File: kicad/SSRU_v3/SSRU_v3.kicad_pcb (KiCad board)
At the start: 2 copper layers, 100 x 100 mm, 122 parts, among them J1 AVR-ISP-6, J10 Conn_01x04, J11 Conn_01x02, J20 Conn_01x02, J21 Conn_01x02, J22 Conn_01x04, J23 Conn_01x02, J24 Conn_01x04, J25 Conn_01x02, J26 Conn_01x03, J27 Conn_01x03, J28 Conn_01x02, J29 Conn_01x02, J3 Conn_01x02, J30 Conn_01x02, J4 Conn_01x02, J5 Conn_01x02, J8 Conn_01x02, J9 Conn_01x02, SW1 SW_Push, U1 MCP2515-xSO, U10 TJA1051T, U11 Ai-Thinker-Ra-02, U12 TJA1051T, U2 ATmega328P-A, U3 TXS0102DCT, U4 LM2576S-5, U5 AMS1117-3.3, U6 LM324, U7 MCP2515-xSO, U8 74LVC1G17, U9 MT3608/SDB628, Y1 16MHz, Y3 16MHz, Y4 16MHz

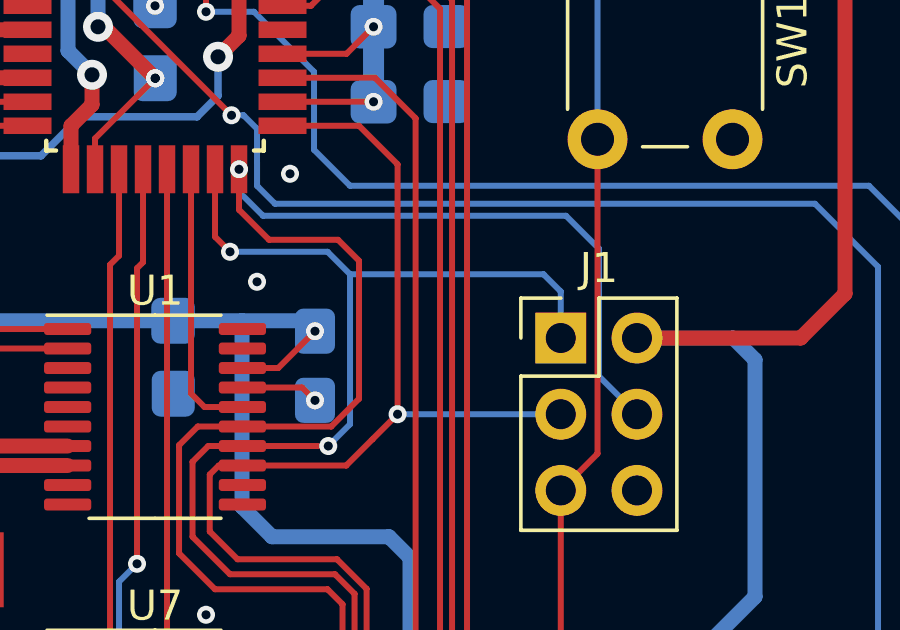
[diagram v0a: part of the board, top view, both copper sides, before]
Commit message: ssru v3
current to voltage lm324 supply to  5v. icsp header mosi miso fixed
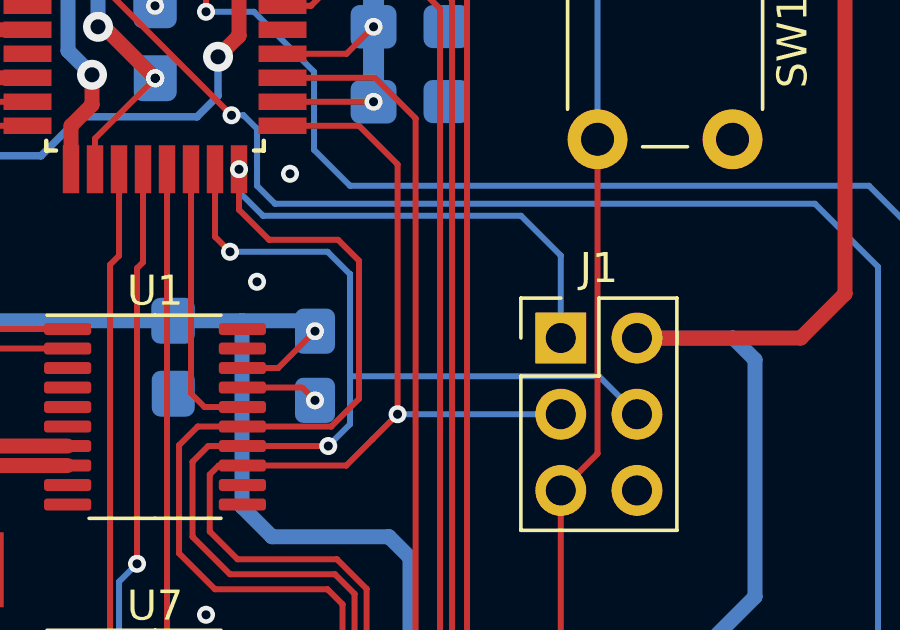
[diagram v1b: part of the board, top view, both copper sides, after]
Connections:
- C21 pad 1: +3.3V -> +5V
- J1 pad 1: MOSI -> MISO
- J1 pad 4: MISO -> MOSI
- U6 pad 4: +3.3V -> +5V
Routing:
- net MOSI: track 78.9 -> 83.6 mm
- net MISO: track 88.4 -> 84.0 mm
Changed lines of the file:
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@@
 			(layers "*.Cu" "*.Mask")
 			(remove_unused_layers no)
-			(net 36 "MOSI")
+			(net 30 "MISO")
 			(pinfunction "MISO")
 			(pintype "passive")
@@
 			(layers "*.Cu" "*.Mask")
 			(remove_unused_layers no)
-			(net 30 "MISO")
+			(net 36 "MOSI")
 			(pinfunction "MOSI")
 			(pintype "passive")
@@
 			(layers "F.Cu" "F.Mask" "F.Paste")
 			(roundrect_rratio 0.15)
-			(net 1 "+3.3V")
+			(net 3 "+5V")
 			(pinfunction "V+")
 			(pintype "power_in")
@@
 			(layers "B.Cu" "B.Mask" "B.Paste")
 			(roundrect_rratio 0.212766)
-			(net 1 "+3.3V")
+			(net 3 "+5V")
 			(pintype "passive")
 		)
@@
 	)
 	(segment
-		(start 164.8 106.9)
-		(end 163.7 105.8)
+		(start 163.525 107.125)
+		(end 162.2 105.8)
 		(width 0.2)
 		(layer "B.Cu")
@@
 	)
 	(segment
-		(start 163.7 105.8)
-		(end 153.6 105.8)
-		(width 0.2)
-		(layer "B.Cu")
-		(net 30)
-	)
-	(segment
-		(start 164.8 111.15)
-		(end 164.8 106.9)
+		(start 153.6 105.8)
+		(end 152.8 105)
 		(width 0.2)
 		(layer "B.Cu")
@@
 	)
 	(segment
-		(start 153.6 105.8)
-		(end 152.8 105)
+		(start 162.2 105.8)
+		(end 153.6 105.8)
 		(width 0.2)
 		(layer "B.Cu")
@@
 	)
 	(segment
-		(start 166.065 112.415)
-		(end 164.8 111.15)
+		(start 163.525 109.875)
+		(end 163.525 107.125)
 		(width 0.2)
 		(layer "B.Cu")
@@
 	(segment
 		(start 156.5 107.75)
-		(end 162.95 107.75)
+		(end 155.75 107)
 		(width 0.2)
 		(layer "B.Cu")
@@
 	)
 	(segment
-		(start 156.5 107.75)
-		(end 155.75 107)
+		(start 164.8 111.15)
+		(end 166.065 112.415)
 		(width 0.2)
 		(layer "B.Cu")
@@
 	)
 	(segment
-		(start 155.75 107)
-		(end 152.5 107)
+		(start 156.5 107.75)
+		(end 156.5 111.15)
 		(width 0.2)
 		(layer "B.Cu")
@@
 	)
 	(segment
-		(start 163.525 108.325)
-		(end 163.525 109.875)
+		(start 155.75 107)
+		(end 152.5 107)
 		(width 0.2)
 		(layer "B.Cu")
@@
 	)
 	(segment
-		(start 162.95 107.75)
-		(end 163.525 108.325)
+		(start 156.5 111.15)
+		(end 164.8 111.15)
 		(width 0.2)
 		(layer "B.Cu")

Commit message: SSRU new layout
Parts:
- removed C37, C47: 100nF, RMC_Capacitor:C_0805_2012Metric_Pad1.18x1.45mm_HandSolder_L
- removed J28, J29: Conn_01x02, Connector_JST:JST_XH_B2B-XH-A_1x02_P2.50mm_Vertical
- added C15: 100nF, RMC_Capacitor:C_0805_2012Metric_Pad1.18x1.45mm_HandSolder_L, B.Cu at (120.0, 127.0)
- added C16: 100nF, RMC_Capacitor:C_0805_2012Metric_Pad1.18x1.45mm_HandSolder_L, B.Cu at (116.0, 127.0)
- added D6: SMA Diode, Diode_SMD:D_SMA_Handsoldering, F.Cu at (125.0, 125.0)
- added F3: Fuse, to be sorted:Fuse_1210_3225Metric_Pad1.42x2.65mm_HandSolder, F.Cu at (125.0, 135.0)
- added J31: Conn_01x04, Connector_JST:JST_XH_B4B-XH-A_1x04_P2.50mm_Vertical, F.Cu at (117.0, 146.0)
- added U13: CH340N, Package_SO:SOP-8_3.9x4.9mm_P1.27mm, F.Cu at (118.0, 134.0)
- C11, C7: footprint Capacitor_THT:CP_Radial_D6.3mm_P2.50mm -> RMC_Capacitor:CP_Radial_D6.3mm_P2.50mm_handsolder
- C28, C29, C31, C36, R1, R28, R29, R30, R31, R32, R33, R34, R35, R37: moved to F.Cu
- C46: value 0.1uF -> 100nF
- F1, F2: footprint Fuse:Fuse_1210_3225Metric_Pad1.42x2.65mm_HandSolder -> to be sorted:Fuse_1210_3225Metric_Pad1.42x2.65mm_HandSolder
- U2: footprint Package_QFP:TQFP-32_7x7mm_P0.8mm -> RMC_QFP:TQFP-32_7x7mm_P0.8mm_L
- U3: footprint Package_SO:SSOP-8_2.95x2.8mm_P0.65mm -> RMC_SO:SOIC-8_3.9x4.9mm_P1.27mm_RMC_Handsolder
- U8: footprint Package_TO_SOT_SMD:SOT-23-5_HandSoldering -> RMC_SOT:SOT-23-5_HandSoldering_Extended_RMC
- U9: footprint Package_TO_SOT_SMD:SOT-23-6_Handsoldering -> RMC_SOT:SOT-23-6_Handsoldering_Extended_RMC
- moved C10 163.0 mm to (53.0, 24.0), turned to -90 degrees
- moved F1 159.4 mm to (48.0, 23.0), turned to -90 degrees
- moved R39 158.7 mm to (55.8, 17.1)
- moved C9 157.4 mm to (56.0, 24.0), turned to 90 degrees
- moved D4 155.9 mm to (62.0, 17.0)
- moved C8 155.2 mm to (55.0, 28.0), turned to 0 degrees
- moved D3 147.8 mm to (54.5, 44.0), turned to -90 degrees
- moved R38 145.9 mm to (51.5, 44.0), turned to -90 degrees
- moved U5 145.3 mm to (65.0, 25.0), turned to 0 degrees
- moved G*** 106.9 mm to (40.1, 96.5)
- moved R23 104.4 mm to (51.0, 66.0), turned to 0 degrees
- moved C35 104.1 mm to (54.0, 60.0), turned to 180 degrees
- moved J30 102.5 mm to (197.0, 84.0)
- moved D5 101.0 mm to (53.0, 57.0), turned to 180 degrees
- moved C33 99.6 mm to (54.0, 63.0), turned to 0 degrees
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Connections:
- net PUMP_THERM_IN renamed PUMP_NTC_100k
- U2 pad 12: LVB_TEMP -> CS_CAN1
- U2 pad 13: CS_CAN1 -> CS_CAN2
- U2 pad 14: CS_CAN2 -> CS_CAN3
- U2 pad 19: POT3_IN -> POT2_IN
- U2 pad 22: POT4_IN -> POT1_IN
- U2 pad 23: POT2_IN -> LVB_TEMP
- U2 pad 24: POT1_IN -> IRO
- U2 pad 30: CS_CAN3 -> 328_RX
- U2 pad 31: IRO -> 328_TX
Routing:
- net +5V: track 362.5 -> 0.00 mm, vias 8 -> 0
- net +3.3V: track 298.4 -> 0.00 mm, vias 8 -> 0
- net RST: track 91.4 -> 0.00 mm, vias 2 -> 0
- net PUMP_NTC_100k: track 85.6 -> 0.00 mm, vias 2 -> 0
- net MISO: track 84.0 -> 0.00 mm, vias 1 -> 0
- net MOSI: track 83.6 -> 0.00 mm, vias 4 -> 0
- net CS_CAN3: track 82.5 -> 0.00 mm, vias 2 -> 0
- net POT3_IN: track 80.2 -> 0.00 mm, vias 1 -> 0
- net POT4_IN: track 78.1 -> 0.00 mm, vias 1 -> 0
- net LVB_TEMP: track 74.2 -> 0.00 mm, vias 3 -> 0
- net SCK: track 73.0 -> 0.00 mm, vias 1 -> 0
- net +24V: track 72.2 -> 0.00 mm
- net POT2_IN: track 71.3 -> 0.00 mm, vias 1 -> 0
- net IRO: track 70.9 -> 0.00 mm, vias 2 -> 0
- net BRAKE_TEMP_OUT4: track 70.0 -> 0.00 mm, vias 4 -> 0
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
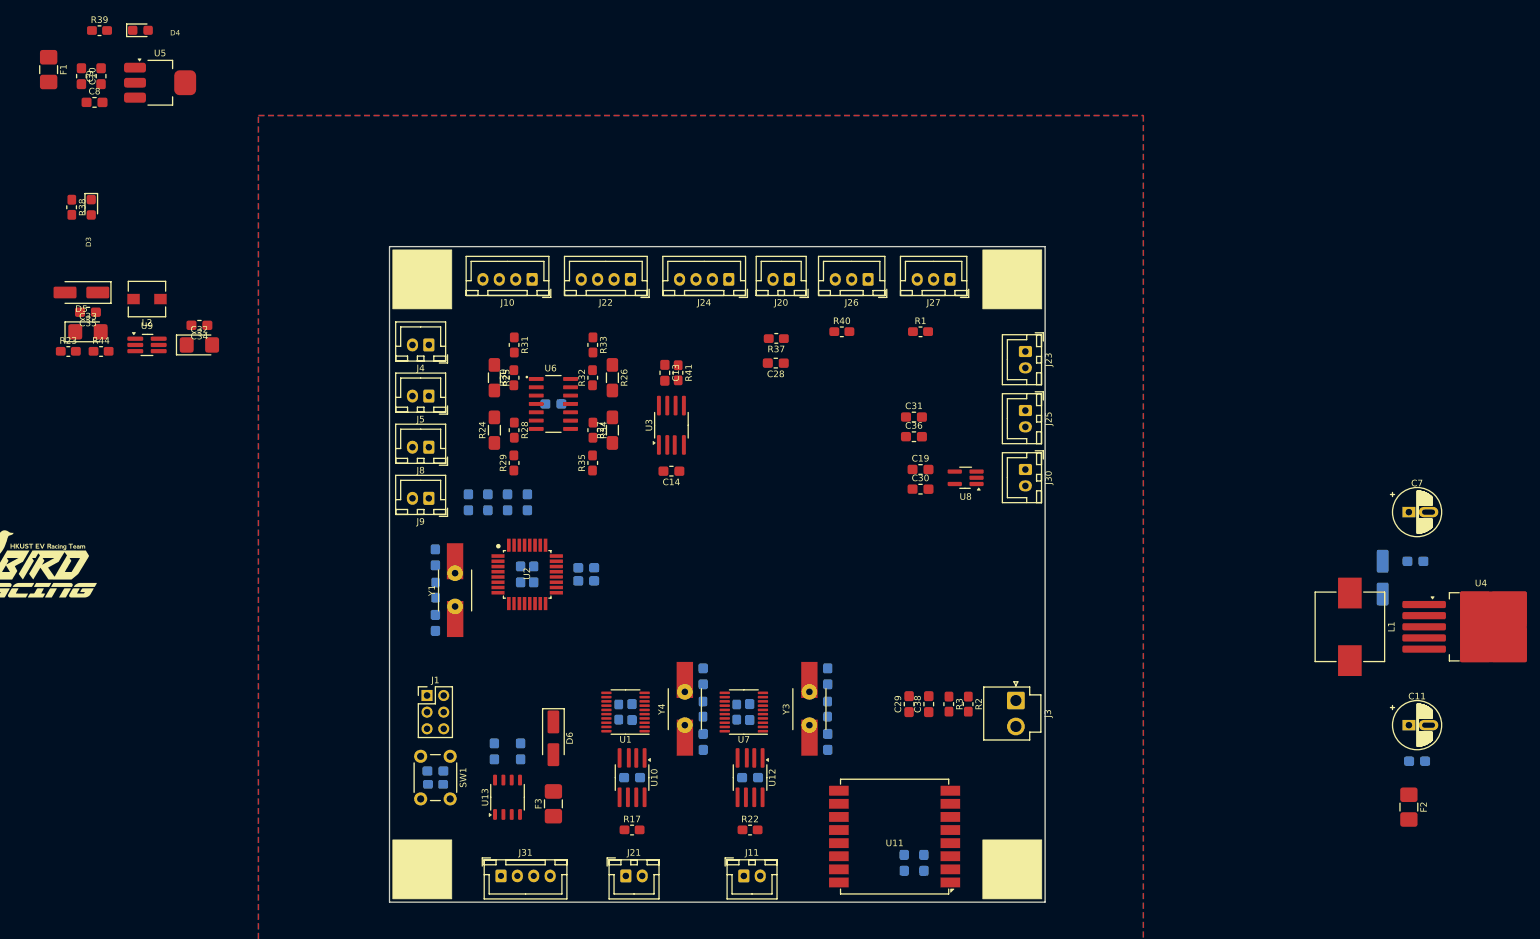
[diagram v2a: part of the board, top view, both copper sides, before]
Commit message: SSRU new scheme
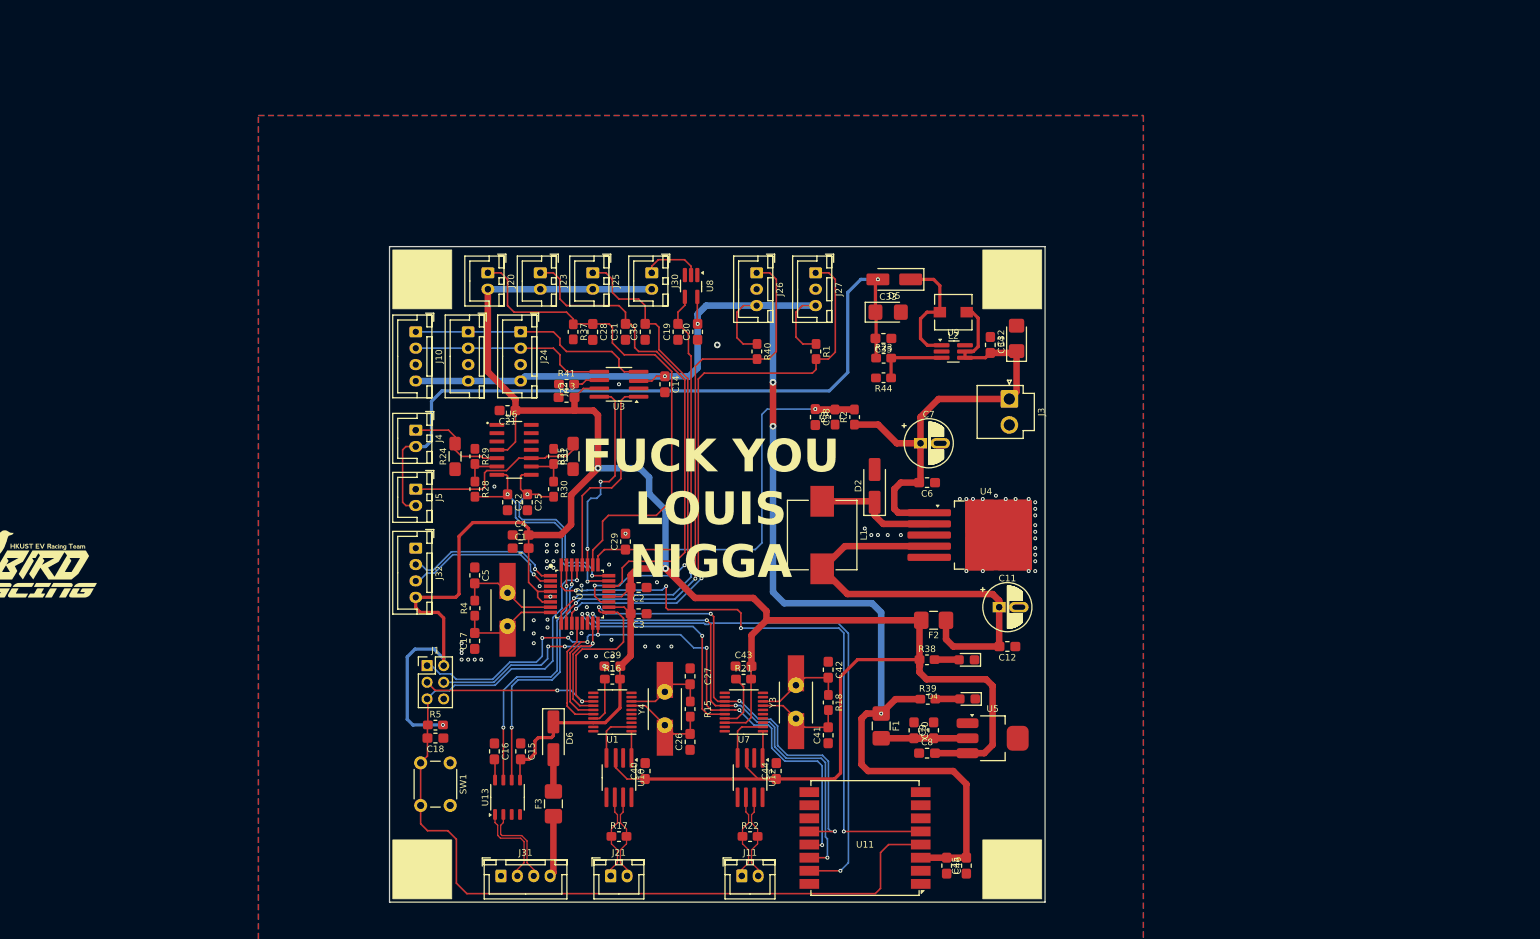
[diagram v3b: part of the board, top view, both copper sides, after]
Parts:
- removed C23, C24: 100nF, RMC_Capacitor:C_0805_2012Metric_Pad1.18x1.45mm_HandSolder_L
- removed J8, J9: Conn_01x02, Connector_JST:JST_XH_B2B-XH-A_1x02_P2.50mm_Vertical
- removed R26, R27: 10R, RMC_Resistor:R_1206_3216Metric_Pad1.30x1.75mm_HandSolder_RMC
- removed R32, R34: 5k, RMC_Resistor:R_0805_2012Metric_Pad1.20x1.40mm_HandSolder_L
- removed R33, R35: 1k, RMC_Resistor:R_0805_2012Metric_Pad1.20x1.40mm_HandSolder_L
- added J32: Conn_01x04, Connector_JST:JST_XH_B4B-XH-A_1x04_P2.50mm_Vertical, F.Cu at (104.0, 96.0)
- C1, C12, C15, C16, C17, C18, C2, C21, C22, C25, C26, C27, C3, C39, C4, C40, C41, C42, C43, C44, C45, C46, C5, C6, D2, R15, R16, R18, R21, R4, R5: moved to F.Cu
- moved R39 162.4 mm to (182.1, 119.1)
- moved D4 162.2 mm to (188.2, 119.0), turned to 180 degrees
- moved F1 161.7 mm to (175.0, 123.1)
- moved U5 161.6 mm to (192.0, 125.0)
- moved C10 161.5 mm to (180.0, 123.8)
- moved C9 161.5 mm to (183.0, 123.8)
- moved C8 161.2 mm to (182.0, 127.3)
- moved D3 150.3 mm to (188.1, 113.0), turned to 180 degrees
- moved R38 147.6 mm to (182.0, 113.0), turned to 0 degrees
- moved C32 124.7 mm to (195.7, 64.0), turned to 90 degrees
- moved R23 124.4 mm to (175.4, 67.0)
- moved D5 124.0 mm to (177.0, 55.0)
- moved L2 123.0 mm to (186.0, 60.0)
- moved U9 123.0 mm to (186.0, 66.0)
- moved C33 122.1 mm to (176.1, 60.0)
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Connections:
- R30 pad 1: Net-(U6A--) -> Net-(U6C--)
- R31 pad 2: Net-(U6A--) -> Net-(U6C--)
- U1 pad 16: CS_CAN2 -> CS_CAN1
- U2 pad 1: BRAKE_TEMP_OUT2 -> ENCODER_A
- U2 pad 10: LVB_S -> Temp_sensor
- U2 pad 11: FLOW_OUT -> LVB_TEMP
- U2 pad 2: BRAKE_TEMP_OUT3 -> ENCODER_B
- U2 pad 23: LVB_TEMP -> BRAKE_TEMP_OUT1
- U2 pad 24: IRO -> BRAKE_TEMP_OUT2
- U2 pad 25: Temp_sensor -> LVB_S
- U2 pad 32: BRAKE_TEMP_OUT1 -> IRO
- U2 pad 9: BRAKE_TEMP_OUT4 -> FLOW_OUT
- U6 pad 1: BRAKE_TEMP_OUT2 -> unconnected-(U6-Pad1)
- U6 pad 10: BRAKE_TEMP4 -> BRAKE_TEMP2
- U6 pad 12: BRAKE_TEMP3 -> unconnected-(U6D-+-Pad12)
- U6 pad 13: Net-(U6D--) -> unconnected-(U6D---Pad13)
- U6 pad 14: BRAKE_TEMP_OUT3 -> unconnected-(U6-Pad14)
- U6 pad 2: Net-(U6A--) -> unconnected-(U6A---Pad2)
- U6 pad 3: BRAKE_TEMP2 -> unconnected-(U6A-+-Pad3)
- U6 pad 8: BRAKE_TEMP_OUT4 -> BRAKE_TEMP_OUT2
- U7 pad 16: CS_CAN1 -> CS_CAN2
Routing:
- net +5V: track 0.00 -> 432.5 mm, vias 0 -> 3
- net +3.3V: track 0.00 -> 232.5 mm, vias 0 -> 5
- net RST: track 0.00 -> 149.2 mm, vias 0 -> 1
- net SCK: track 0.00 -> 119.6 mm, vias 0 -> 6
- net +24V: track 0.00 -> 116.3 mm, vias 0 -> 1
- net MOSI: track 0.00 -> 115.8 mm, vias 0 -> 7
- net MISO: track 0.00 -> 112.6 mm, vias 0 -> 7
- net IRO: track 0.00 -> 95.2 mm, vias 0 -> 4
- net LVB_TEMP: track 0.00 -> 92.2 mm, vias 0 -> 2
- net CS_CAN3: track 0.00 -> 84.2 mm, vias 0 -> 2
- net Temp_sensor: track 0.00 -> 83.1 mm, vias 0 -> 2
- net PUMP_NTC_100k: track 0.00 -> 77.3 mm
- net POT1_IN: track 0.00 -> 74.7 mm
- net +12V: track 0.00 -> 74.6 mm
- net POT2_IN: track 0.00 -> 73.8 mm, vias 0 -> 2
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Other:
- board text added: "FUCK YOU LOUIS NIGGA"

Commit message: SSRU
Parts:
- moved G*** 121.1 mm to (161.0, 104.4)
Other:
- board text added: "3V3"
- board text added: "GND"
- board text added: "PUMP POT1 POT2 FLOW"
- board text added: "SCL"
- board text added: "SDA"
